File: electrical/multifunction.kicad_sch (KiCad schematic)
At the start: 32 parts

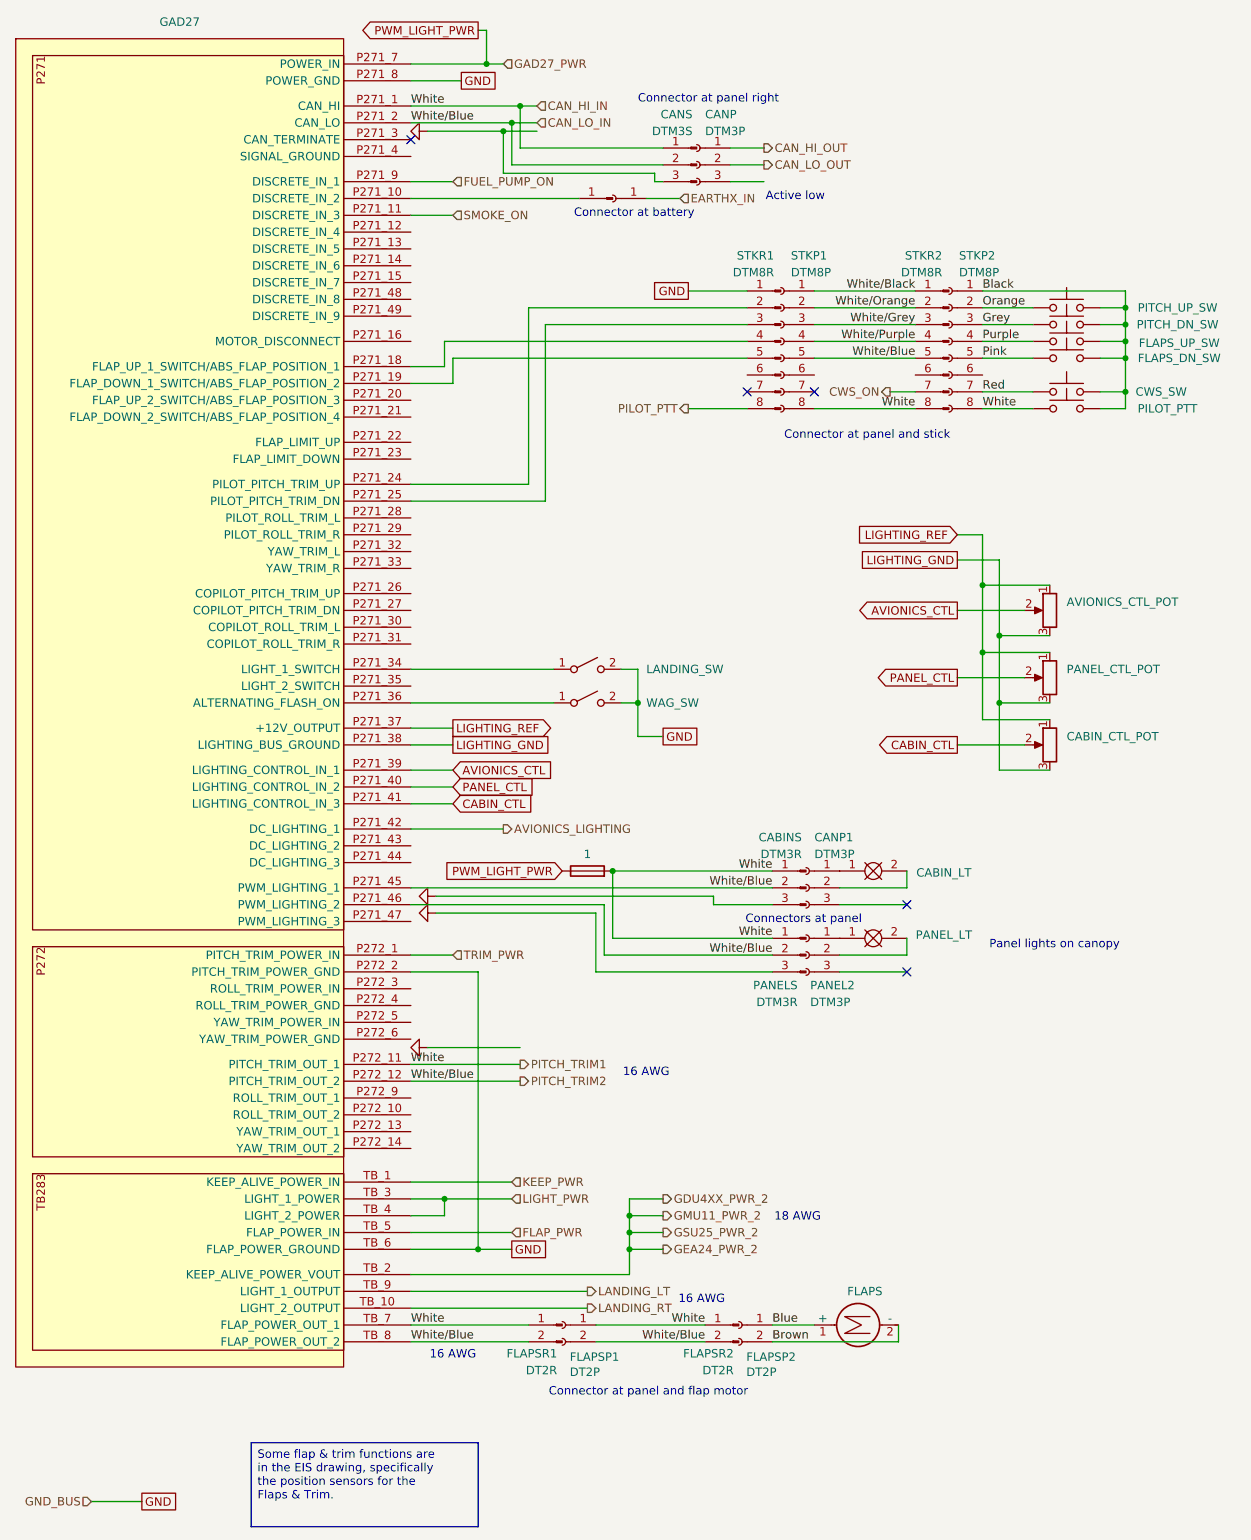
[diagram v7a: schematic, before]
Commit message: Assumed engine connector is sufficient for wiring on bench..
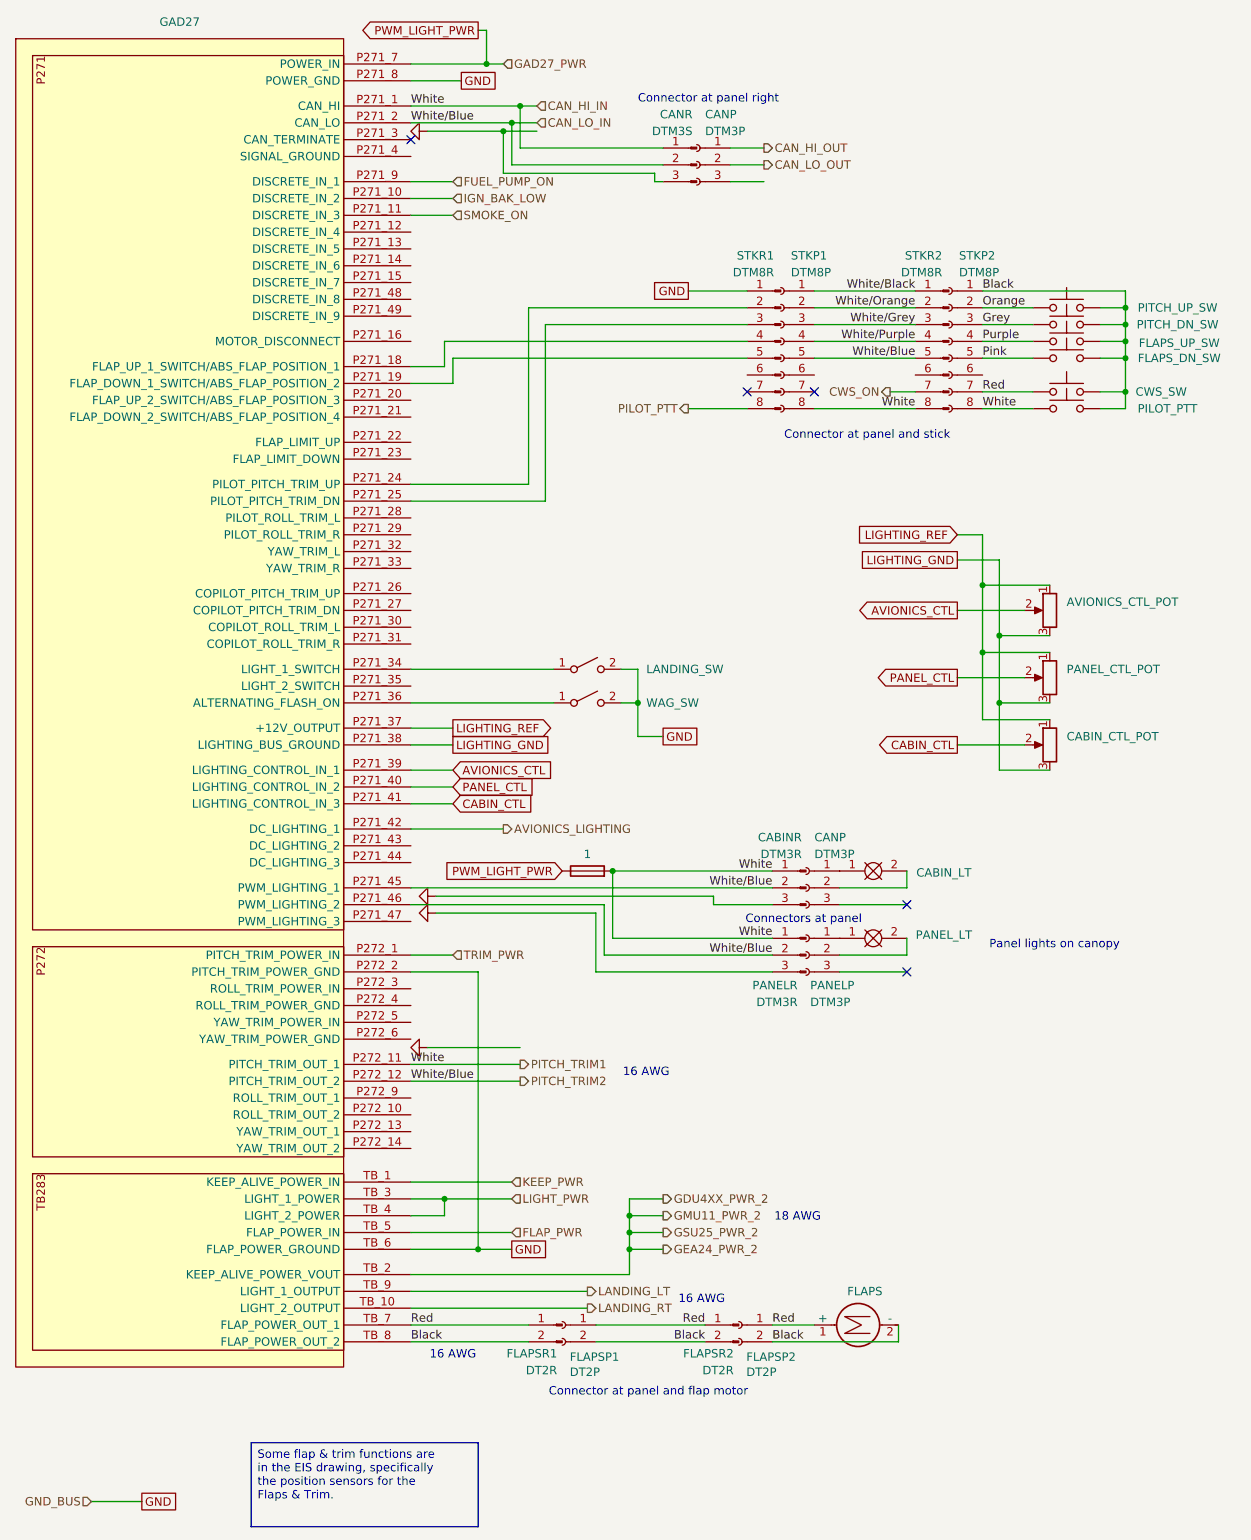
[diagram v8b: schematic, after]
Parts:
- removed EARTHXP: Conn_01x01_Pin, symbol Connector:Conn_01x01_Pin
- removed EARTHXS: Conn_01x01_Socket, symbol Connector:Conn_01x01_Socket
- renumbered CABINS to CABINR, CANP1 to CANP, CANS to CANR, PANEL2 to PANELP, PANELS to PANELR
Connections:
- net Blue is gone; now on net Red: FLAPS.1 (+), FLAPSP2.1 (Pin_1)
- net Brown is gone; now on net Black: FLAPS.2 (-), FLAPSP2.2 (Pin_2)
- net Black: now also FLAPSP1.2 (Pin_2), FLAPSR1.2 (Pin_2), FLAPSR2.2 (Pin_2), GAD27.TB_8 (FLAP_POWER_OUT_2)
- net CAN_HI_IN: no longer FLAPSP1.1 (Pin_1), FLAPSR1.1 (Pin_1), FLAPSR2.1 (Pin_1), GAD27.TB_7 (FLAP_POWER_OUT_1)
- net CAN_LO_IN: no longer FLAPSP1.2 (Pin_2), FLAPSR1.2 (Pin_2), FLAPSR2.2 (Pin_2), GAD27.TB_8 (FLAP_POWER_OUT_2)
- net Red: now also FLAPSP1.1 (Pin_1), FLAPSR1.1 (Pin_1), FLAPSR2.1 (Pin_1), GAD27.TB_7 (FLAP_POWER_OUT_1)
- net IGN_BAK_LOW: now reaches GAD27.P271_10 (DISCRETE_IN_2)
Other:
- note removed: "Active low"
- note removed: "Connector at battery"
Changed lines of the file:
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@@
 		)
 	)
-	(text "Connector at battery"
-		(exclude_from_sim no)
-		(at 105.918 49.276 0)
-		(effects
-			(font
-				(size 1.27 1.27)
-			)
-			(justify left)
-		)
-	)
 	(text "16 AWG"
 		(exclude_from_sim no)
@@
 		)
 	)
-	(text "Active low"
-		(exclude_from_sim no)
-		(at 134.874 46.736 0)
-		(effects
-			(font
-				(size 1.27 1.27)
-			)
-			(justify left)
-		)
-	)
 	(text_box "Some flap & trim functions are in the EIS drawing, specifically the position sensors for the Flaps & Trim."
 		(exclude_from_sim no)
@@
 	(wire
 		(pts
+			(xy 81.28 49.53) (xy 87.63 49.53)
+		)
+		(stroke
+			(width 0)
+			(type default)
+		)
+	)
+	(wire
+		(pts
 			(xy 135.89 161.29) (xy 110.49 161.29)
 		)
@@
 	(wire
 		(pts
-			(xy 81.28 49.53) (xy 87.63 49.53)
-		)
-		(stroke
-			(width 0)
-			(type default)
-		)
-	)
-	(wire
-		(pts
 			(xy 189.23 63.5) (xy 189.23 66.04)
 		)
@@
 	(wire
 		(pts
-			(xy 81.28 46.99) (xy 106.68 46.99)
+			(xy 167.64 105.41) (xy 177.8 105.41)
 		)
 		(stroke
@@
 	(wire
 		(pts
-			(xy 167.64 105.41) (xy 177.8 105.41)
+			(xy 81.28 46.99) (xy 87.63 46.99)
 		)
 		(stroke
@@
 	(wire
 		(pts
-			(xy 116.84 46.99) (xy 121.92 46.99)
-		)
-		(stroke
-			(width 0)
-			(type default)
-		)
-	)
-	(wire
-		(pts
 			(xy 114.3 205.74) (xy 114.3 209.55)
 		)
@@
 		)
 	)
-	(label "White"
+	(label "Red"
 		(at 81.28 217.17 0)
 		(effects
@@
 		)
 	)
-	(label "Blue"
+	(label "Red"
 		(at 135.89 217.17 0)
 		(effects
@@
 		)
 	)
-	(label "White"
+	(label "Red"
 		(at 125.73 217.17 180)
 		(effects
@@
 		)
 	)
-	(label "Brown"
+	(label "Black"
 		(at 135.89 219.71 0)
 		(effects
@@
 		)
 	)
-	(label "White{slash}Blue"
+	(label "Black"
 		(at 81.28 219.71 0)
 		(effects
@@
 		)
 	)
-	(label "White{slash}Blue"
+	(label "Black"
 		(at 125.73 219.71 180)
 		(effects
@@
 		)
 	)
-	(hierarchical_label "KEEP_PWR"
+	(hierarchical_label "IGN_BAK_LOW"
 		(shape input)
-		(at 96.52 195.58 0)
+		(at 87.63 46.99 0)
 		(effects
 			(font
@@
 		)
 	)
-	(hierarchical_label "FLAP_PWR"
+	(hierarchical_label "KEEP_PWR"
 		(shape input)
-		(at 96.52 203.2 0)
+		(at 96.52 195.58 0)
 		(effects
 			(font
@@
 		)
 	)
-	(hierarchical_label "FUEL_PUMP_ON"
+	(hierarchical_label "FLAP_PWR"
 		(shape input)
-		(at 87.63 44.45 0)
+		(at 96.52 203.2 0)
 		(effects
 			(font
@@
 		)
 	)
-	(hierarchical_label "EARTHX_IN"
+	(hierarchical_label "FUEL_PUMP_ON"
 		(shape input)
-		(at 121.92 46.99 0)
+		(at 87.63 44.45 0)
 		(effects
 			(font
@@
 		(on_board yes)
 		(dnp no)
-		(property "Reference" "CANS"
+		(property "Reference" "CANR"
 			(at 123.825 34.29 0)
 			(effects
@@
 			(project ""
 				(path "/e8ec215a-dbe2-4eba-a577-e50a0a128049/67540fe5-9b6d-4d8c-9d03-cde1487f48ae"
-					(reference "CANS")
+					(reference "CANR")
 					(unit 1)
 				)
@@
 		(on_board yes)
 		(dnp no)
-		(property "Reference" "CANP1"
+		(property "Reference" "CANP"
 			(at 142.24 143.51 0)
 			(effects
@@
 			(project "electrical"
 				(path "/e8ec215a-dbe2-4eba-a577-e50a0a128049/67540fe5-9b6d-4d8c-9d03-cde1487f48ae"
-					(reference "CANP1")
+					(reference "CANP")
 					(unit 1)
 				)
@@
 		(on_board yes)
 		(dnp no)
-		(property "Reference" "CABINS"
+		(property "Reference" "CABINR"
 			(at 140.335 143.51 0)
 			(effects
@@
 			(project "electrical"
 				(path "/e8ec215a-dbe2-4eba-a577-e50a0a128049/67540fe5-9b6d-4d8c-9d03-cde1487f48ae"
-					(reference "CABINS")
-					(unit 1)
-				)
-			)
-		)
-	)
-	(symbol
-		(lib_id "Connector:Conn_01x01_Socket")
-		(at 111.76 46.99 0)
-		(mirror y)
-		(unit 1)
-		(exclude_from_sim no)
-		(in_bom yes)
-		(on_board yes)
-		(dnp no)
-		(fields_autoplaced yes)
-		(property "Reference" "EARTHXS"
-			(at 110.49 45.7199 0)
-			(effects
-				(font
-					(size 1.27 1.27)
-				)
-				(justify left)
-				(hide yes)
-			)
-		)
-		(property "Value" "Conn_01x01_Socket"
-			(at 110.49 46.9899 0)
-			(effects
-				(font
-					(size 1.27 1.27)
-				)
-				(justify left)
-				(hide yes)
-			)
-		)
-		(property "Footprint" ""
-			(at 111.76 46.99 0)
-			(effects
-				(font
-					(size 1.27 1.27)
-				)
-				(hide yes)
-			)
-		)
-		(property "Datasheet" "~"
-			(at 111.76 46.99 0)
-			(effects
-				(font
-					(size 1.27 1.27)
-				)
-				(hide yes)
-			)
-		)
-		(property "Description" "Generic connector, single row, 01x01, script generated"
-			(at 111.76 46.99 0)
-			(effects
-				(font
-					(size 1.27 1.27)
-				)
-				(hide yes)
-			)
-		)
-		(pin "1"
-		)
-		(instances
-			(project ""
-				(path "/e8ec215a-dbe2-4eba-a577-e50a0a128049/67540fe5-9b6d-4d8c-9d03-cde1487f48ae"
-					(reference "EARTHXS")
+					(reference "CABINR")
 					(unit 1)
 				)
@@
 		(on_board yes)
 		(dnp no)
-		(property "Reference" "PANELS"
+		(property "Reference" "PANELR"
 			(at 139.7 165.862 0)
 			(effects
@@
 			(project "electrical"
 				(path "/e8ec215a-dbe2-4eba-a577-e50a0a128049/67540fe5-9b6d-4d8c-9d03-cde1487f48ae"
-					(reference "PANELS")
+					(reference "PANELR")
 					(unit 1)
 				)
@@
 		(on_board yes)
 		(dnp no)
-		(property "Reference" "PANEL2"
+		(property "Reference" "PANELP"
 			(at 141.605 165.862 0)
 			(effects
@@
 			(project "electrical"
 				(path "/e8ec215a-dbe2-4eba-a577-e50a0a128049/67540fe5-9b6d-4d8c-9d03-cde1487f48ae"
-					(reference "PANEL2")
+					(reference "PANELP")
 					(unit 1)
 				)
@@
 					(unit 1)
 				)
-			)
-		)
-	)
-	(symbol
-		(lib_id "Connector:Conn_01x01_Pin")
-		(at 111.76 46.99 0)
-		(mirror y)
-		(unit 1)
-		(exclude_from_sim no)
-		(in_bom yes)
-		(on_board yes)
-		(dnp no)
-		(fields_autoplaced yes)
-		(property "Reference" "EARTHXP"
-			(at 111.125 41.91 0)
-			(effects
-				(font
-					(size 1.27 1.27)
-				)
-				(hide yes)
-			)
-		)
-		(property "Value" "Conn_01x01_Pin"
-			(at 111.125 44.45 0)
-			(effects
-				(font
-					(size 1.27 1.27)
-				)
-				(hide yes)
-			)
-		)
-		(property "Footprint" ""
-			(at 111.76 46.99 0)
-			(effects
-				(font
-					(size 1.27 1.27)
-				)
-				(hide yes)
-			)
-		)
-		(property "Datasheet" "~"
-			(at 111.76 46.99 0)
-			(effects
-				(font
-					(size 1.27 1.27)
-				)
-				(hide yes)
-			)
-		)
-		(property "Description" "Generic connector, single row, 01x01, script generated"
-			(at 111.76 46.99 0)
-			(effects
-				(font
-					(size 1.27 1.27)
-				)
-				(hide yes)
-			)
-		)
-		(pin "1"
-		)
-		(instances
-			(project ""
-				(path "/e8ec215a-dbe2-4eba-a577-e50a0a128049/67540fe5-9b6d-4d8c-9d03-cde1487f48ae"
-					(reference "EARTHXP")
-					(unit 1)
-				)
